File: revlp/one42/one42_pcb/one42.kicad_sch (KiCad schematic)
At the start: 37 parts, among them J1 Conn_01x04_Female, Q1 AO3401A, SW44 SW_SPDT, U1 TP4054, U2 AP2112K-3.3, U3 nRF52840_holyiot_18010, U4 One42

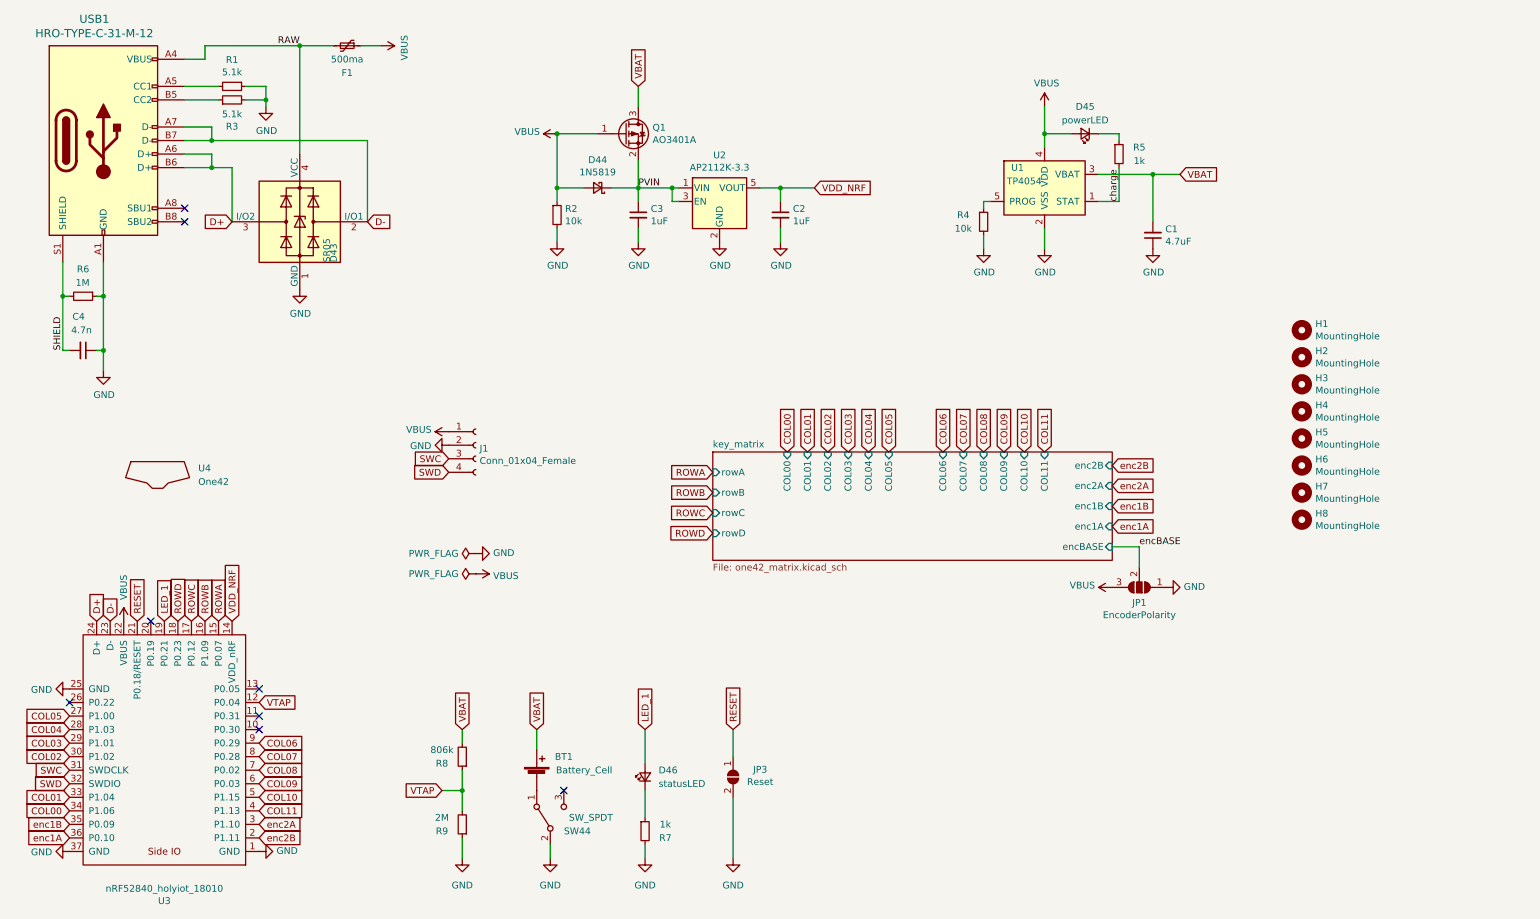
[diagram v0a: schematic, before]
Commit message: [project] One42: Update schematic & PDF
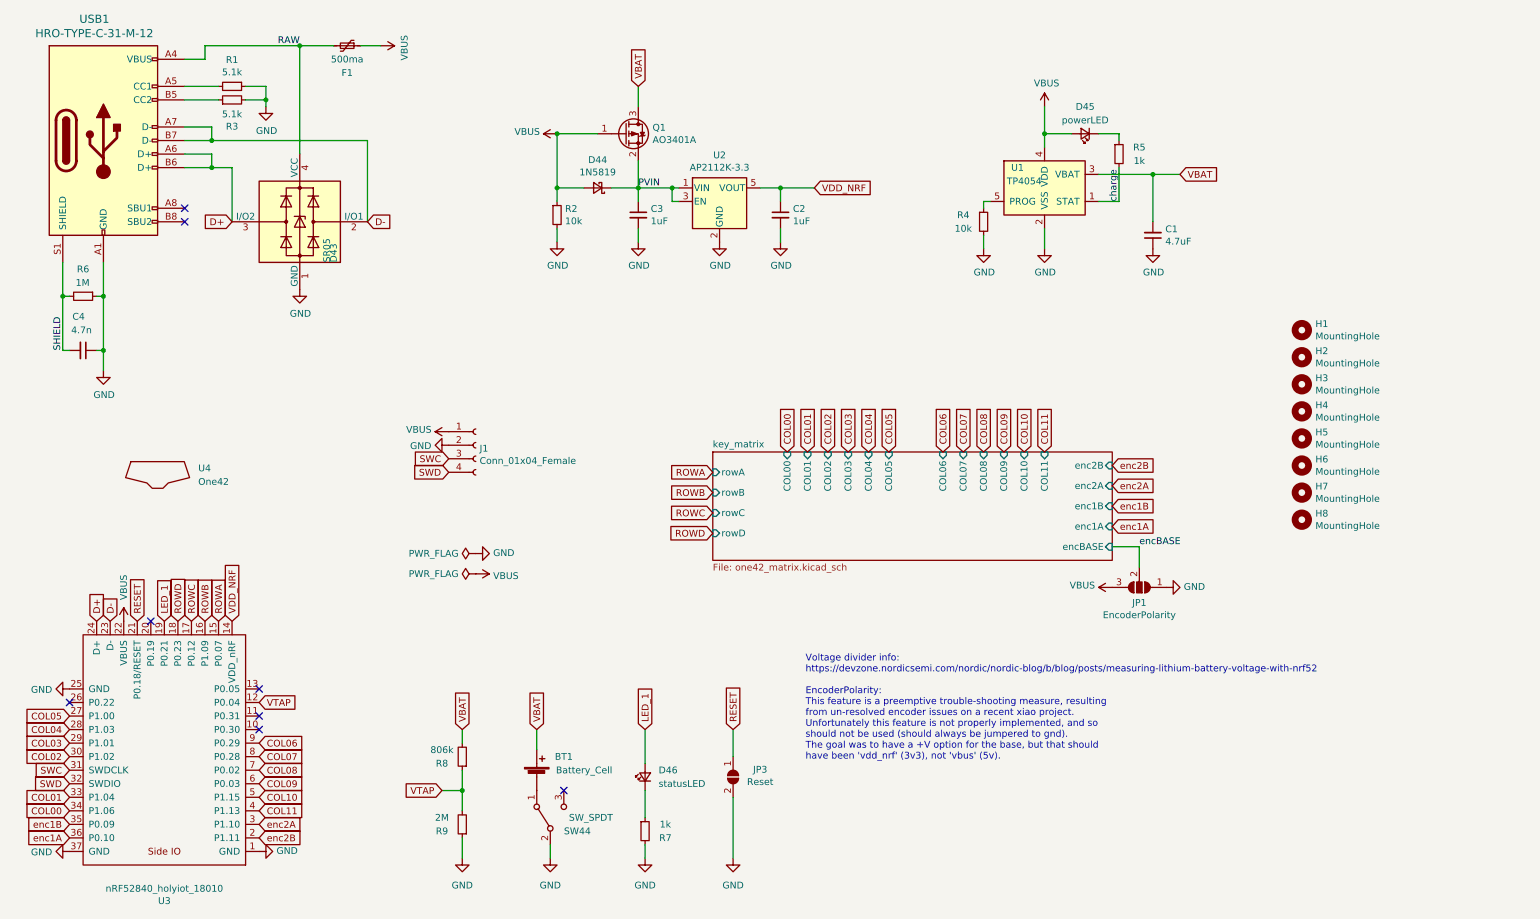
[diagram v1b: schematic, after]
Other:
- note added: "Voltage divider info: https://devzone.nordicsemi.com/nordic/nordic-blog/b/blog/posts/measuring-lithium-battery-voltage-with-nrf52 EncoderPolarity: This feature is a preemptive trouble-shooting measure, resulting from un-resolved encoder issues on a recent xiao project. Unfortunately this feature is not properly implemented, and so should not be used (should always be jumpered to gnd). The goal wa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"
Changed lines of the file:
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@@
     (stroke (width 0) (type default) (color 0 0 0 0))
+  )
+  (text "Voltage divider info:\nhttps://devzone.nordicsemi.com/nordic/nordic-blog/b/blog/posts/measuring-lithium-battery-voltage-with-nrf52\n\nEncoderPolarity:\nThis feature is a preemptive trouble-shooting measure, resulting\nfrom un-resolved encoder issues on a recent xiao project.\nUnfortunately this feature is not properly implemented, and so\nshould not be used (should always be jumpered to gnd).\nThe goal was to have a +V option for the base, but that should\nhave been 'vdd_nrf' (3v3), not 'vbus' (5v).\n"
+    (at 169.799 162.052 0)
+    (effects (font (size 1.27 1.27)) (justify left bottom))
   )
   (label "SHIELD" (at 30.48 85.09 90)
